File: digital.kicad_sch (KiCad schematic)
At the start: 24 parts

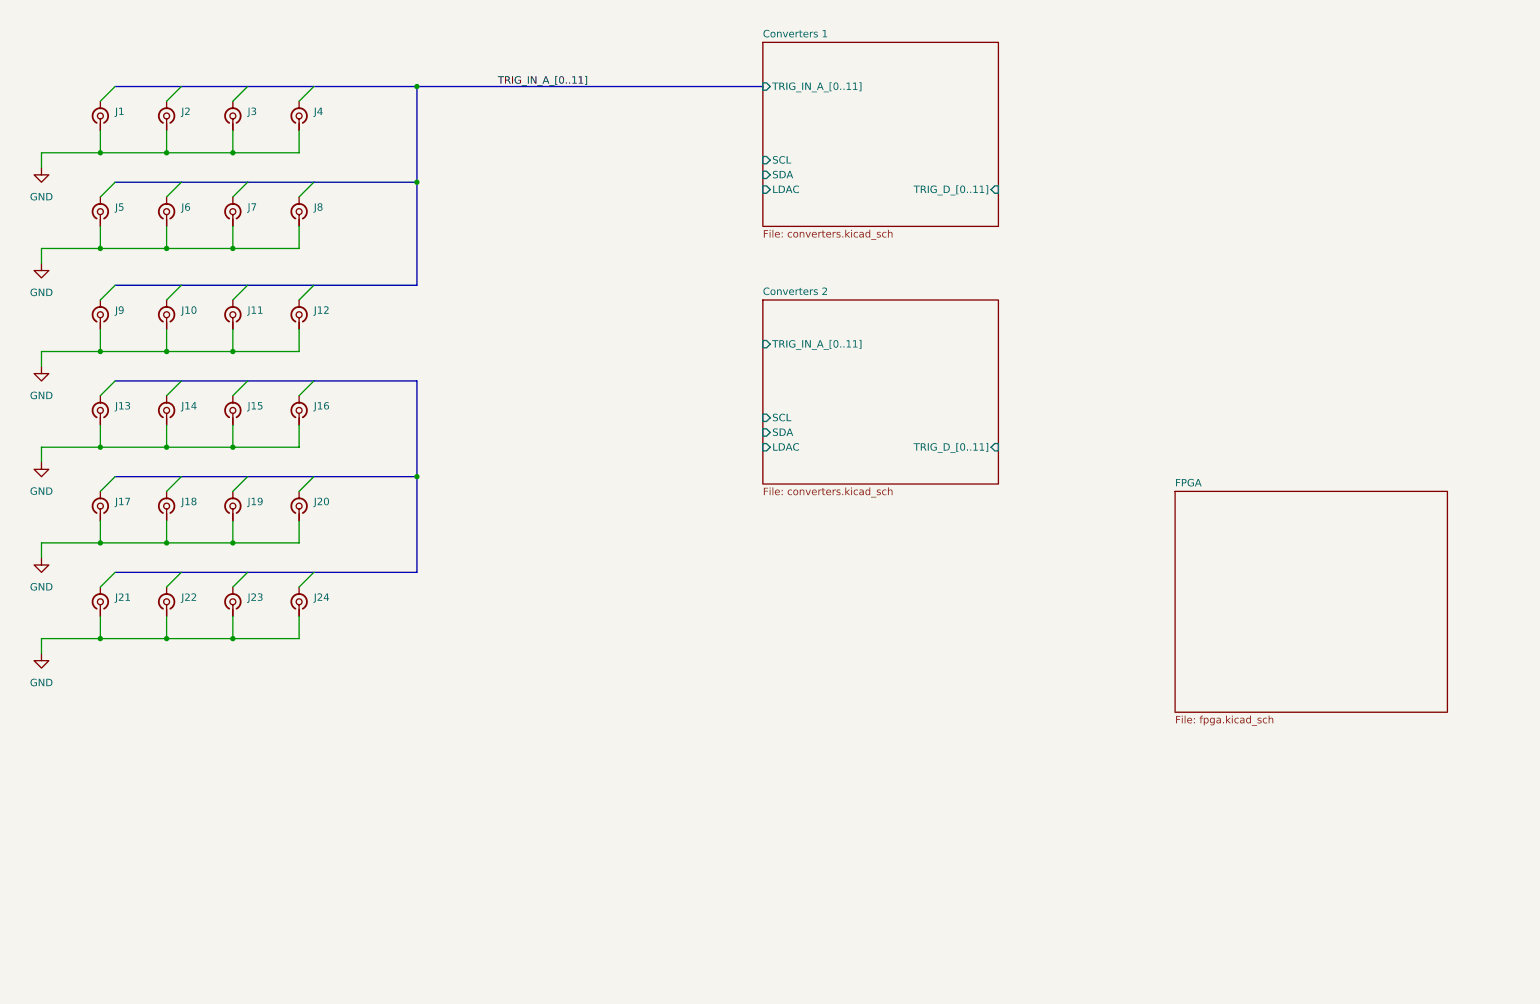
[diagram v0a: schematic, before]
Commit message: Added SD card readers and USB-C for power in.
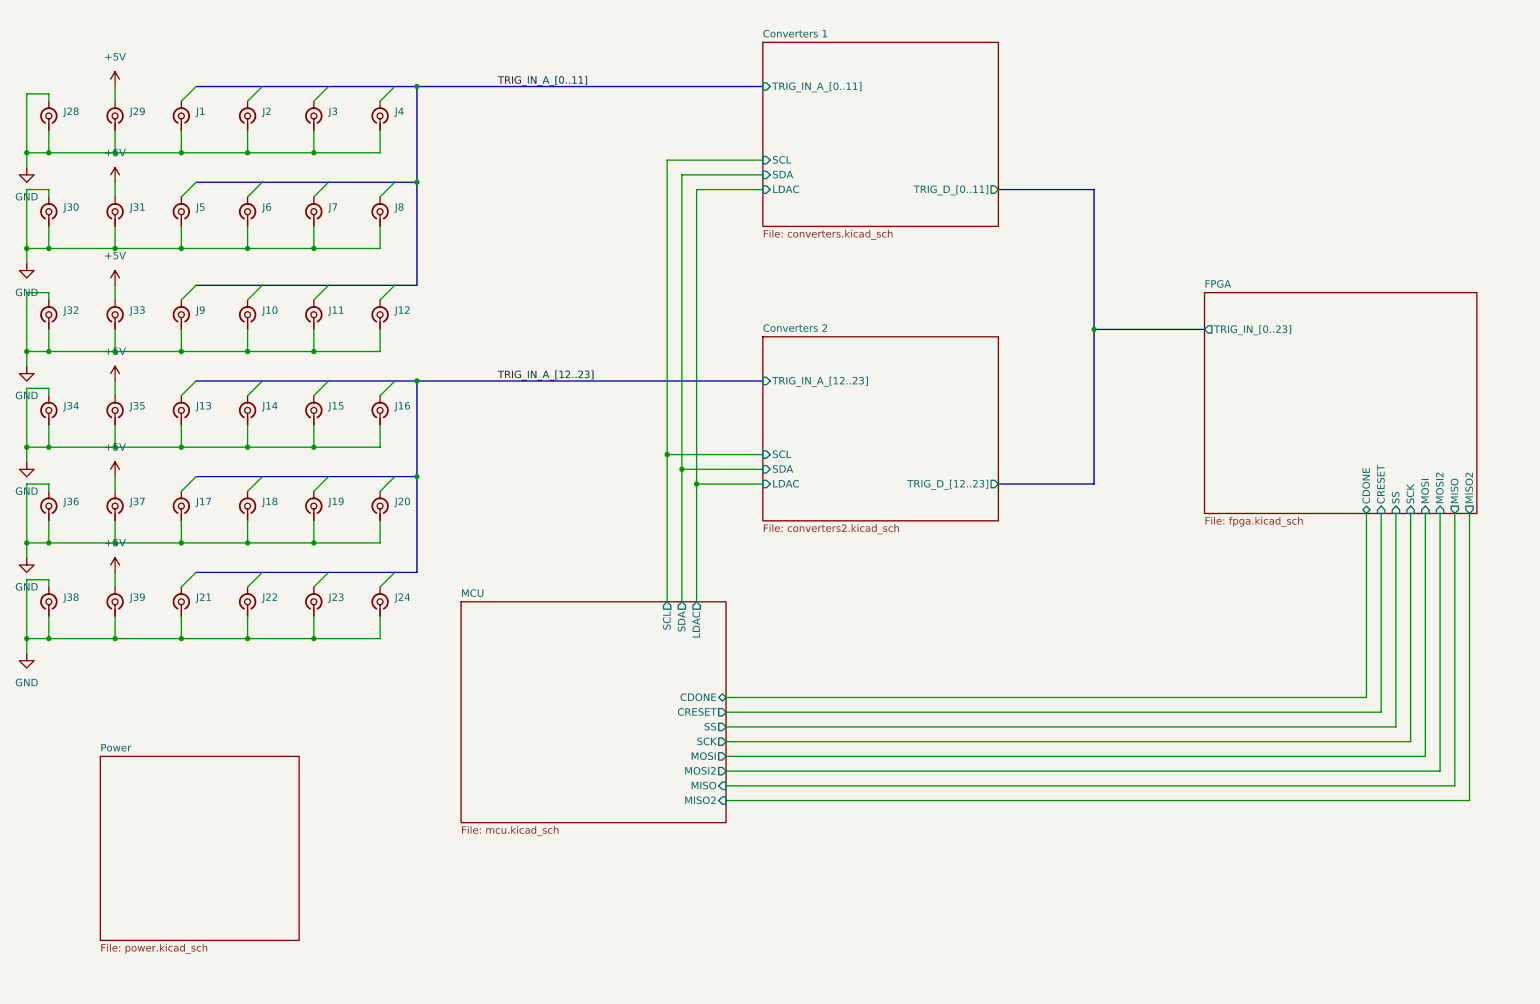
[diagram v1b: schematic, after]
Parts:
- added J28, J29, J30, J31, J32, J33, J34, J35, J36, J37, J38, J39: ~, symbol Connector:Conn_Coaxial_Small
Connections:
- net GND: now also J28.1 (In), J28.2 (Ext), J29.1 (In), J30.1 (In), J30.2 (Ext), J31.1 (In), J32.1 (In), J32.2 (Ext), J33.1 (In), J34.1 (In), J34.2 (Ext), J35.1 (In), J36.1 (In), J36.2 (Ext), J37.1 (In), J38.1 (In), J38.2 (Ext), J39.1 (In)
- new net +5V: J29.2 (Ext), J31.2 (Ext), J33.2 (Ext), J35.2 (Ext), J37.2 (Ext), J39.2 (Ext)
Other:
- added sheet MCU (mcu.kicad_sch)
- added sheet Power (power.kicad_sch)
- sheet Converters 2: file converters.kicad_sch -> converters2.kicad_sch
- sheet Converters 2 ports: added TRIG_D_[12..23], TRIG_IN_A_[12..23]; removed TRIG_D_[0..11], TRIG_IN_A_[0..11]
- sheet FPGA ports: added CDONE, CRESET, MISO, MISO2, MOSI, MOSI2, SCK, SS, TRIG_IN_[0..23]; removed none
- moved on the sheet: J1, J10, J11, J12, J13, J14, J15, J16, J17, J18, J19, J2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

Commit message: generate pdfs
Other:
- note added: "SMA CONNECTORS INPUT"
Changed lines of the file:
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@@
 	(generator_version "9.0")
 	(paper "A4")
+	(text "SMA CONNECTORS INPUT"
+		(exclude_from_sim no)
+		(at 59.69 30.48 0)
+		(effects
+			(font
+				(size 1.27 1.27)
+			)
+		)
+	)
 	(junction
 		(at 72.39 62.23)

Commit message: Small aesthetic changes and small rework of power sheet.
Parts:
- removed J28, J29, J30, J31, J32, J33, J34, J35, J36, J37, J38, J39: ~, symbol Connector:Conn_Coaxial_Small
- added H1, H2, H3, H4, H5, H6: M3, symbol Mechanical:MountingHole_Pad
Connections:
- new net GNDPWR: H1.1, H2.1, H3.1, H4.1, H5.1, H6.1
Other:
- note removed: "SMA CONNECTORS INPUT"
- moved on the sheet: J1, J10, J11, J12, J13, J14, J15, J16, J17, J18, J19, J2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

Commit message: complete power
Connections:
- net GND: now also J1.2 (Ext), J10.2 (Ext), J11.2 (Ext), J12.2 (Ext), J13.2 (Ext), J14.2 (Ext), J15.2 (Ext), J16.2 (Ext), J17.2 (Ext), J18.2 (Ext), J19.2 (Ext), J2.2 (Ext), J20.2 (Ext), J21.2 (Ext), J22.2 (Ext), J23.2 (Ext), J24.2 (Ext), J3.2 (Ext), J4.2 (Ext), J5.2 (Ext), J6.2 (Ext), J7.2 (Ext), J8.2 (Ext), J9.2 (Ext); no longer J1.1 (In), J10.1 (In), J11.1 (In), J12.1 (In), J13.1 (In), J14.1 (In), J15.1 (In), J16.1 (In), J17.1 (In), J18.1 (In), J19.1 (In), J2.1 (In), J20.1 (In), J21.1 (In), J22.1 (In), J23.1 (In), J24.1 (In), J3.1 (In), J4.1 (In), J5.1 (In), J6.1 (In), J7.1 (In), J8.1 (In), J9.1 (In)
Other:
- sheet Power renamed power
- added sheet power_sipm (power_sipm.kicad_sch)
- added sheet usb (usb.kicad_sch)
- moved on the sheet: J1, J10, J11, J12, J13, J14, J15, J16, J17, J18, J19, J2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

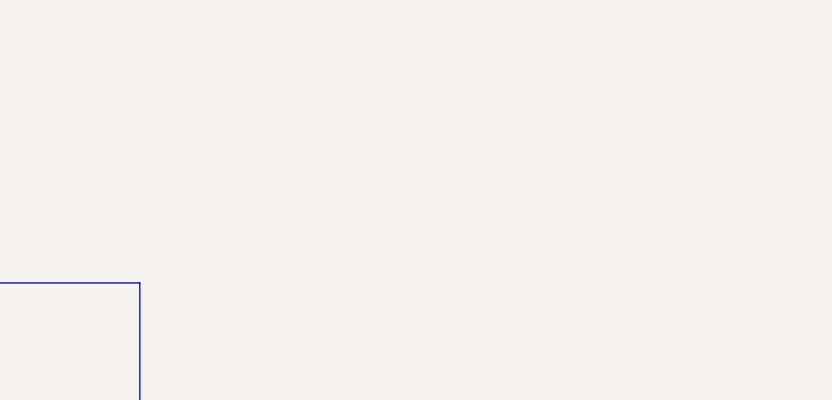
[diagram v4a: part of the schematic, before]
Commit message: reroute dac + comparators
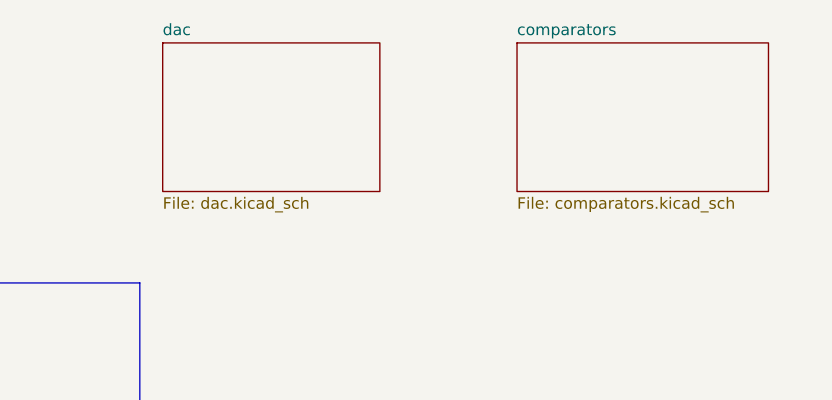
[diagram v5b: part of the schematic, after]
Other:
- added sheet comparators (comparators.kicad_sch)
- added sheet dac (dac.kicad_sch)
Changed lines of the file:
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@@
+	)
+	(sheet
+		(at 248.92 24.13)
+		(size 27.94 16.51)
+		(exclude_from_sim no)
+		(in_bom yes)
+		(on_board yes)
+		(dnp no)
+		(fields_autoplaced yes)
+		(stroke
+			(width 0.1524)
+			(type solid)
+		)
+		(fill
+			(color 0 0 0 0.0000)
+		)
+		(property "Sheetname" "comparators"
+			(at 248.92 23.4184 0)
+			(effects
+				(font
+					(size 1.27 1.27)
+				)
+				(justify left bottom)
+			)
+		)
+		(property "Sheetfile" "comparators.kicad_sch"
+			(at 248.92 41.2246 0)
+			(effects
+				(font
+					(size 1.27 1.27)
+				)
+				(justify left top)
+			)
+		)
+		(instances
+			(project "digital"
+				(path "/4c5c7ce5-09d6-4a32-b2a0-f32b0c47f27d"
+					(page "10")
+				)
+			)
+		)
+	)
+	(sheet
+		(at 209.55 24.13)
+		(size 24.13 16.51)
+		(exclude_from_sim no)
+		(in_bom yes)
+		(on_board yes)
+		(dnp no)
+		(fields_autoplaced yes)
+		(stroke
+			(width 0.1524)
+			(type solid)
+		)
+		(fill
+			(color 0 0 0 0.0000)
+		)
+		(property "Sheetname" "dac"
+			(at 209.55 23.4184 0)
+			(effects
+				(font
+					(size 1.27 1.27)
+				)
+				(justify left bottom)
+			)
+		)
+		(property "Sheetfile" "dac.kicad_sch"
+			(at 209.55 41.2246 0)
+			(effects
+				(font
+					(size 1.27 1.27)
+				)
+				(justify left top)
+			)
+		)
+		(instances
+			(project "digital"
+				(path "/4c5c7ce5-09d6-4a32-b2a0-f32b0c47f27d"
+					(page "9")
+				)
+			)
+		)
 	)
 	(sheet

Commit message: cleanup
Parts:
- removed J1, J10, J11, J12, J13, J14, J15, J16, J17, J18, J19, J2, J20, J21, J22, J23, J24, J3, J4, J5, J6, J7, J8, J9: ~, symbol Connector:Conn_Coaxial_Small
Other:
- removed sheet Converters 1
- removed sheet Converters 2
- sheet FPGA ports: added none; removed TRIG_IN_[0..23]
- sheet dac ports: added VREF_SCL, VREF_SDA, ~{LDAC}[0..5]; removed none

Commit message: rewire
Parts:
- removed H1, H2, H3, H4, H5, H6: M3, symbol Mechanical:MountingHole_Pad
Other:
- sheet MCU ports: added none; removed CDONE, CRESET, LDAC, MISO, MISO2, MOSI, MOSI2, SCK, SCL, SDA, SS
